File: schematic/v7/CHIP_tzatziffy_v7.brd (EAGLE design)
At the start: 40.9 x 49.8 mm, 60 parts, among them J1 2X20-CHIP0.7_DRILL, Q2 n.a. / 2N7002ET1G, U1 n.a. / LMR62421, U3 DS2431P, X1 FH12-40S-0.5SH

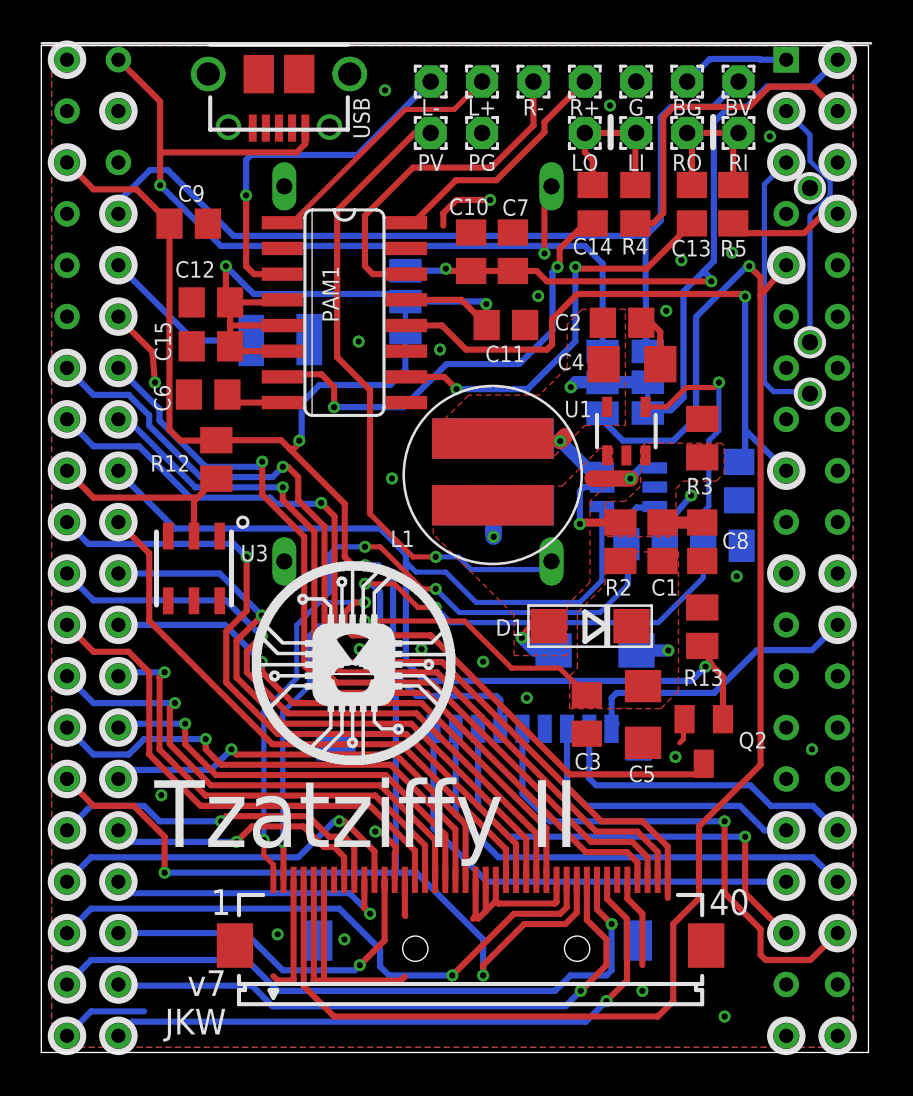
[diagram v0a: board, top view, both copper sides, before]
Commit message: improved routing
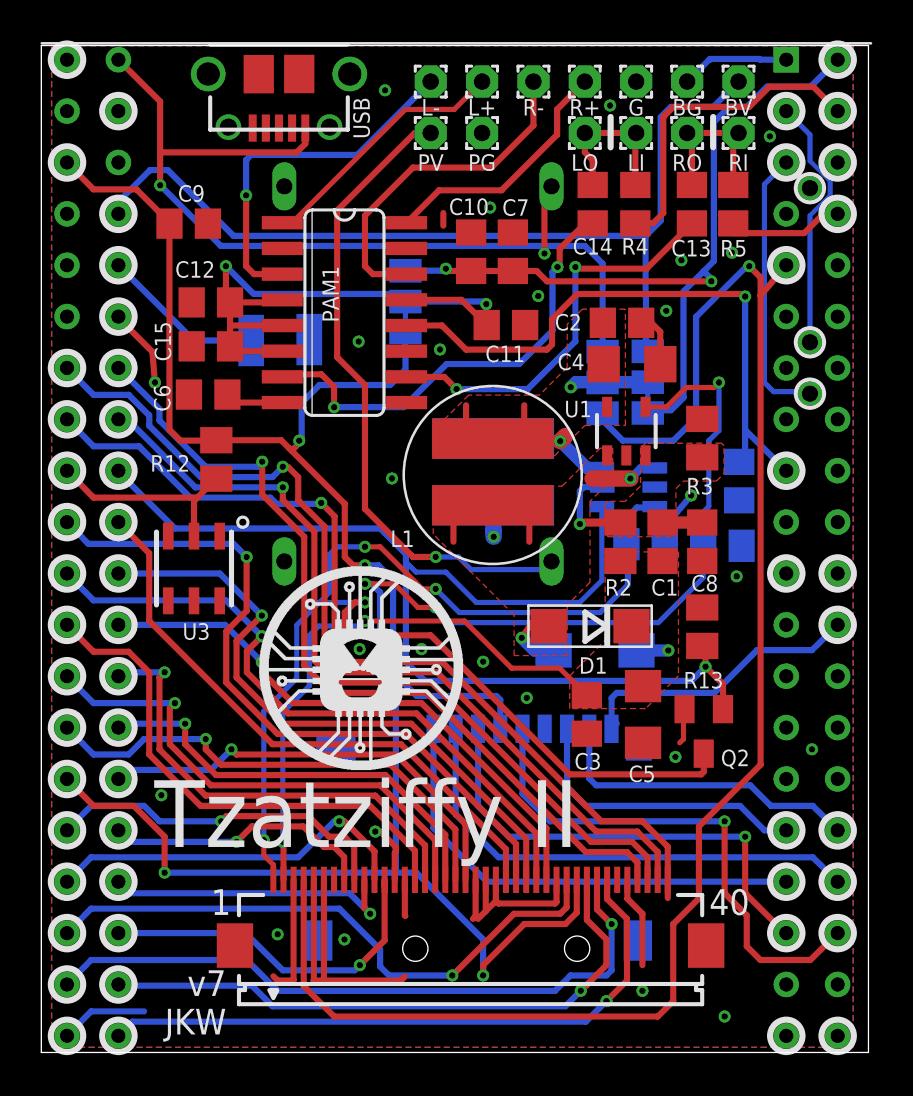
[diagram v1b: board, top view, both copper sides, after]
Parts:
- moved Q2 0.50 mm to (32.8, 15.9)
- moved U$2 0.45 mm to (10.8, 14.0)
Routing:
- net VREG_OUTPUT: track 7.59 -> 10.1 mm
- net GND: track 63.6 -> 61.5 mm
- net DC_IN: track 10.9 -> 12.9 mm
- net R+OUT: track 12.2 -> 13.0 mm
- net PWM: track 55.9 -> 55.1 mm
